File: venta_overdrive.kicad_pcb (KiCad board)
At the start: 2 copper layers, 50 x 54 mm, 46 parts, among them J1 IN, J2 OUT, J3 9V, J4 GND, J5 GND, J6 LED-, U1 JRC4558D, U2 JRC4558D, U3 JRC4558D

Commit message: pcb lint
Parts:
- moved J3 0.60 mm to (96.6, 62.6)
- moved J4 0.60 mm to (103.4, 62.6)
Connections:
- net +9V_IN renamed /+9V_IN
- net BP renamed /BP
- net BUF_IN renamed /BUF_IN
- net BUF_OUT renamed /BUF_OUT
- net CLIP renamed /CLIP
- net DRIVE_HI renamed /DRIVE_HI
- net DRIVE_W renamed /DRIVE_W
- net EQ_A renamed /EQ_A
- net EQ_B renamed /EQ_B
- net GAIN_FB renamed /GAIN_FB
- net GAIN_OUT renamed /GAIN_OUT
- net GAIN_RC renamed /GAIN_RC
- net GND renamed /GND
- net HP renamed /HP
- net IN renamed /IN
- net INT1_N renamed /INT1_N
- net INT2_N renamed /INT2_N
- net LED_A renamed /LED_A
- net LED_K renamed /LED_K
- net LP renamed /LP
- net LP_AC renamed /LP_AC
- net OUT renamed /OUT
- net OUT_DC renamed /OUT_DC
- net RES renamed /RES
- net SUM renamed /SUM
- net VB renamed /VB
- net VCC renamed /VCC
- net VOL_HI renamed /VOL_HI
- net VOL_W renamed /VOL_W
- net VREF renamed /VREF
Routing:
- net /VCC: track 66.6 -> 75.9 mm
- net /VREF: track 45.0 -> 49.3 mm
- net /RES: track 38.0 -> 40.7 mm, vias 2 -> 3
- net /INT2_N: track 11.4 -> 13.7 mm, vias 2 -> 0
- net /INT1_N: track 40.1 -> 39.3 mm
- net /BP: track 59.9 -> 60.6 mm, vias 4 -> 3
- net /+9V_IN: track 7.97 -> 8.47 mm
- net /HP: vias 2 -> 0

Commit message: use external LED
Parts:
- removed the J1 at (121.0, 111.0)
- removed R17: 3.3k, Resistor_SMD:R_0805_2012Metric
- added J7: GND, Venta:WirePad, F.Cu at (91.0, 111.0)
- J1: renamed from D4; value LED red 5mm -> IN; footprint LED_THT:LED_D5.0mm -> Venta:WirePad
- J6: value LED- -> LED+
- moved J1 22.8 mm to (121.0, 111.0)
- moved J6 3.00 mm to (97.0, 111.0)
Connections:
- J1 pad 1: /LED_K -> /IN
- J6 pad 1: /LED_K -> /VCC
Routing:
- net /VCC: track 75.9 -> 85.4 mm
- net /LED_K: track 4.95 -> 0.00 mm
- net /GND: track 131.1 -> 134.3 mm
- net /LED_A: track 1.75 -> 0.00 mm

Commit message: fix R8 nominal
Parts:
- R8: value 15k -> 75k

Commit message: fix Resonance direction
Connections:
- RV2 pad 1: /RES -> /BP
- RV2 pad 3: /BP -> /RES
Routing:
- net /BP: track 60.6 -> 50.2 mm
- net /RES: track 40.7 -> 42.3 mm

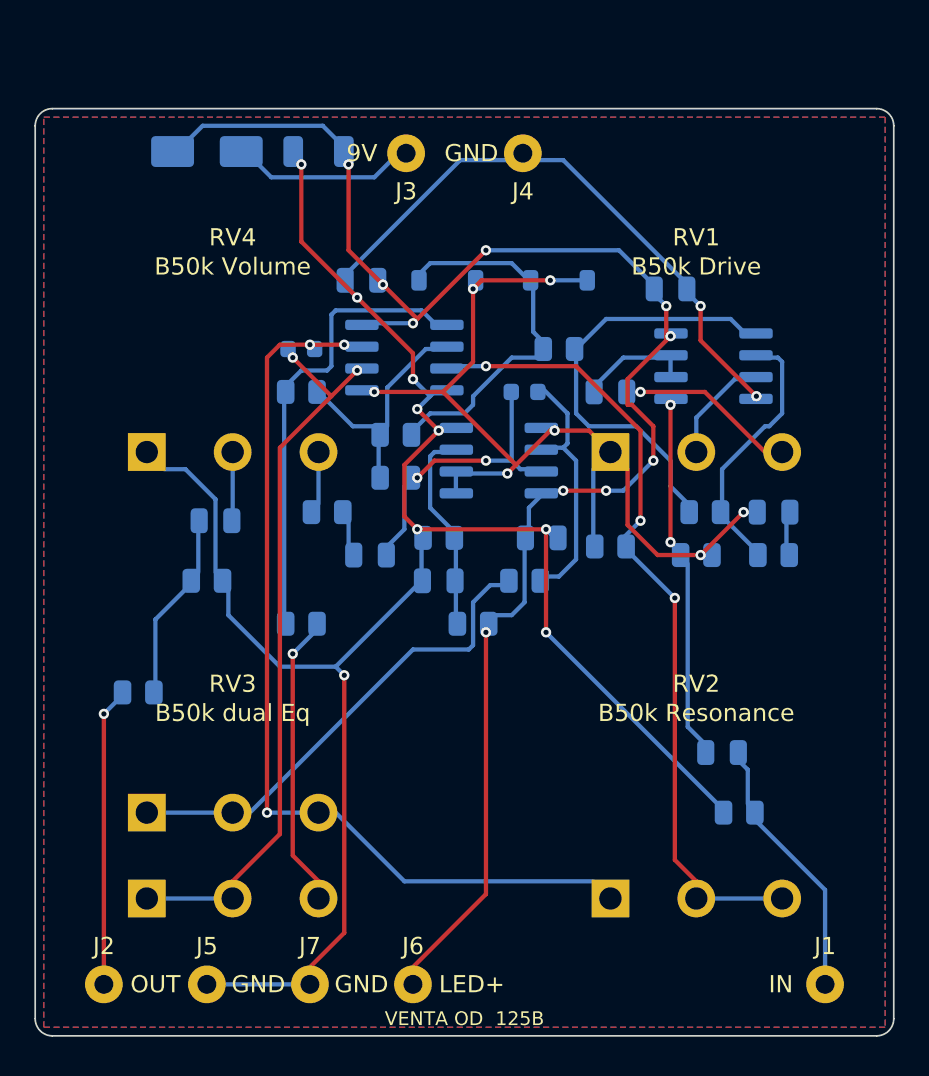
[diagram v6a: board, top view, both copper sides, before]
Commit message: adjust board for dual-gang pot
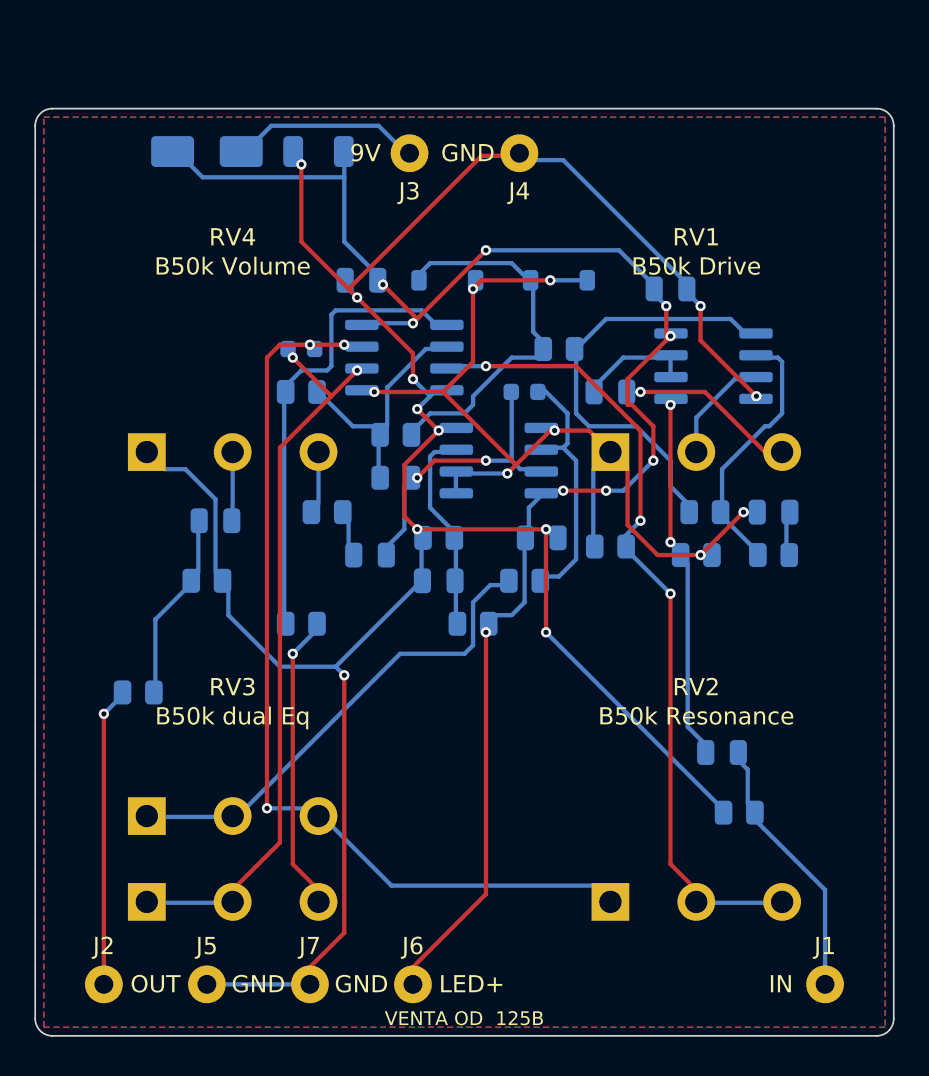
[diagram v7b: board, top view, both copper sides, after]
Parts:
- moved J3 0.20 mm to (96.8, 62.6)
- moved J4 0.20 mm to (103.2, 62.6)
- moved RV2 0.20 mm to (113.5, 90.2)
- moved RV3 0.20 mm to (86.5, 90.2)
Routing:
- net /VCC: track 85.4 -> 84.7 mm, vias 10 -> 9
- net /RES: track 42.3 -> 42.9 mm
- net /GND: track 134.3 -> 134.9 mm
